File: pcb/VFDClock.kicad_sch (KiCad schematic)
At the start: 80 parts, among them J1 Conn_02x03_Top_Bottom_Mountin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, J2 Conn_02x03_Top_Bottom_Mountin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, J3 USB_C_Receptacle_USB2.0_16P, J4 Conn_02x03_Top_Bottom_Mountin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, J5 Conn_02x03_Top_Bottom_Mountin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, Q1 BSS138, SW1 SW_SPST, SW2 SW_SPST, SW3 SW_SPST, SW4 SW_SPST, SW5 SW_SPST, SW6 SW_SPST, U1 TBD62783AFWG, U10 IP4234CZ6, U11 DS3231MZ+TRL, U2 ESP32-S3-WROOM-1, U3 TBD62783AFNG, U4 SN74HC595PWR, U5 AMS1117-3.3, U6 SHT45-AD1B-R2, U7 AMS1117-1.5, U8 VEML3235SL

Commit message: Added footprints
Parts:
- removed D35: 1PS70SB84, Package_TO_SOT_SMD:SOT-323_SC-70, symbol Diode:BAT54SW
- removed J1, J2, J4, J5: Conn_02x03_Top_Bottom_MountingPin, symbol Connector_Generic_MountingPin:Conn_02x03_Top_Bottom_MountingPin
- removed SW1: SW_SPST, Button_Switch_SMD:SW_SPST_B3U-1000P, symbol Switch:SW_SPST
- added C10, C11, C12, C13: 100n, Capacitor_SMD:C_0805_2012Metric, symbol Device:C
- added C21: 22u, Capacitor_Tantalum_SMD:CP_EIA-3528-15_AVX-H, symbol Device:C_Polarized
- added F1: 3,5 A, Fuse:Fuseholder_Cylinder-5x20mm_Schurter_0031_8201_Horizontal_Open, symbol Device:Fuse
- added J1: Conn_01x04_Socket, Connector_PinSocket_2.54mm:PinSocket_2x02_P2.54mm_Vertical_SMD, symbol Connector:Conn_01x04_Socket
- added J2: L_SIG_CONN, Connector_PinHeader_2.54mm:PinHeader_2x03_P2.54mm_Horizontal, symbol Connector_Generic:Conn_02x03_Top_Bottom
- added J3: L_PWR_CONN, Connector_PinHeader_2.54mm:PinHeader_2x03_P2.54mm_Horizontal, symbol Connector_Generic:Conn_02x03_Top_Bottom
- added J5: R_SIG_CONN, Connector_PinHeader_2.54mm:PinHeader_2x03_P2.54mm_Horizontal, symbol Connector_Generic:Conn_02x03_Top_Bottom
- added J6: R_PWR_CONN, Connector_PinHeader_2.54mm:PinHeader_2x03_P2.54mm_Horizontal, symbol Connector_Generic:Conn_02x03_Top_Bottom
- added J7: Conn_02x06_Top_Bottom, Connector_PinSocket_2.54mm:PinSocket_2x06_P2.54mm_Vertical_SMD, symbol Connector_Generic:Conn_02x06_Top_Bottom
- added SW2: SW_SPST, Button_Switch_SMD:SW_SPST_PTS810, symbol Switch:SW_SPST
- BT1: value Battery_Cell -> CR2032; footprint (none) -> Battery:BatteryHolder_Keystone_3034_1x20mm
- D1: renamed from D3; footprint (none) -> Diode_SMD:D_0603_1608Metric
- D2: footprint (none) -> Diode_SMD:D_0603_1608Metric
- R19: renamed from R21; footprint (none) -> OptoDevice:R_LDR_5.1x4.3mm_P3.4mm_Vertical
- RV1: footprint (none) -> Potentiometer_THT:Potentiometer_Bourns_3339P_Vertical
- SW1: renamed from SW2; footprint Button_Switch_SMD:SW_SPST_B3U-1000P -> Button_Switch_SMD:SW_SPST_PTS810
- SW3, SW4, SW5, SW6: footprint (none) -> Button_Switch_THT:SW_Tactile_SPST_Angled_PTS645Vx83-2LFS
- renumbered C5 to C14, C8 to C15, C13 to C16, C11 to C17, C12 to C18, C9 to C19, C10 to C20, C6 to C5, C7 to C6, C14 to C7, C15 to C8, C16 to C9, D25 to D10, D26 to D11, D33 to D12, D34 to D13, D30 to D3, D27 to D4, D28 to D5, D31 to D6, D32 to D7, D19 to D8, D20 to D9, J3 to J4, R13 to R1, R2 to R10, R3 to R11, R4 to R12, R5 to R13, R6 to R14, R9 to R15, R10 to R16, R11 to R17, R12 to R18, R14 to R2, R7 to R20, R8 to R21, R15 to R3, R16 to R4, R17 to R5, R18 to R6, R19 to R7, R20 to R8, R1 to R9, U7 to U10, U10 to U3, U3 to U4, U4 to U5, U5 to U6, U11 to U7, U6 to U8, U8 to U9
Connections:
- net +3V3: now also J1.1 (Pin_1), J7.1 (Pin_1)
- net +5V: now also C10.1, C11.1, C12.1, C13.1, F1.1, J3.1 (Pin_1), J3.2 (Pin_2), J3.3 (Pin_3), J6.1 (Pin_1), J6.2 (Pin_2), J6.3 (Pin_3), J7.7 (Pin_7); no longer U3.5 (VP)
- net GND: now also C10.2, C11.2, C12.2, C13.2, C21.2, J1.4 (Pin_4), J3.4 (Pin_4), J3.5 (Pin_5), J3.6 (Pin_6), J6.4 (Pin_4), J6.5 (Pin_5), J6.6 (Pin_6), J7.11 (Pin_11), J7.12 (Pin_12), J7.6 (Pin_6), SW2.2 (B)
- net GRID_L1: now also J2.1 (Pin_1)
- net GRID_L2: now also J2.2 (Pin_2)
- net GRID_R1: now also J5.1 (Pin_1)
- net GRID_R2: now also J5.2 (Pin_2)
- net RCLK: now also J2.6 (Pin_6), J5.6 (Pin_6)
- net SER_LEFT: now also J2.3 (Pin_3)
- net SER_RIGHT: now also J5.3 (Pin_3)
- net SRCLK: now also J2.4 (Pin_4), J5.4 (Pin_4)
- net Uphoto: now also U2.8 (IO15)
- net Vbat: now also C21.1
- net /SRCLR: now also J2.5 (Pin_5), J5.5 (Pin_5)
- net at R12.2: now also SW2.1 (A)
- net GPIO3: now reaches U2.15 (IO3)
- net GPIO3: now also J7.2 (Pin_2)
- net GPIO48: now reaches U2.25 (IO48)
- net GPIO48: now also J7.10 (Pin_10)
- net GPIO40: now reaches U2.33 (IO40)
- net GPIO40: now also J7.5 (Pin_5)
- net GPIO41: now reaches U2.34 (IO41)
- net GPIO41: now also J7.8 (Pin_8)
- net GPIO42: now reaches U2.35 (IO42)
- net GPIO42: now also J7.9 (Pin_9)
- net at U2.36 (RXD0): now also J1.3 (Pin_3)
- net at U2.37 (TXD0): now also J1.2 (Pin_2)
- net GPIO16: now reaches U2.9 (IO16)
- net GPIO16: now also J7.3 (Pin_3)
- net TEMP_DATA renamed GPIO39
- net GPIO39: now also J7.4 (Pin_4)
- new net: F1.2, U3.5 (VP)
- no-connect marks 16 -> 12
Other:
- note added: "0,25 mA"
- note added: "0,33 mA"
- note added: "0,5 mA"
- note added: "0,65 mA"
- note added: "144 mA (5 V)"
- note added: "3 mA (25,5 V)"
- note added: "360 mW bez ESP"
- note added: "37 mA"
- note added: "70 mA"
- note added: "Left display connectors"
- note added: "Neopixel decoupling"
- note added: "Right display connectors"
- note added: "UART"
- note removed: "Power budget na 3V3 Board interconnecty"
- moved on the sheet: BT1, C1, C14, C15, C16, C17, C18, C19, C2, C20, C3, C4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

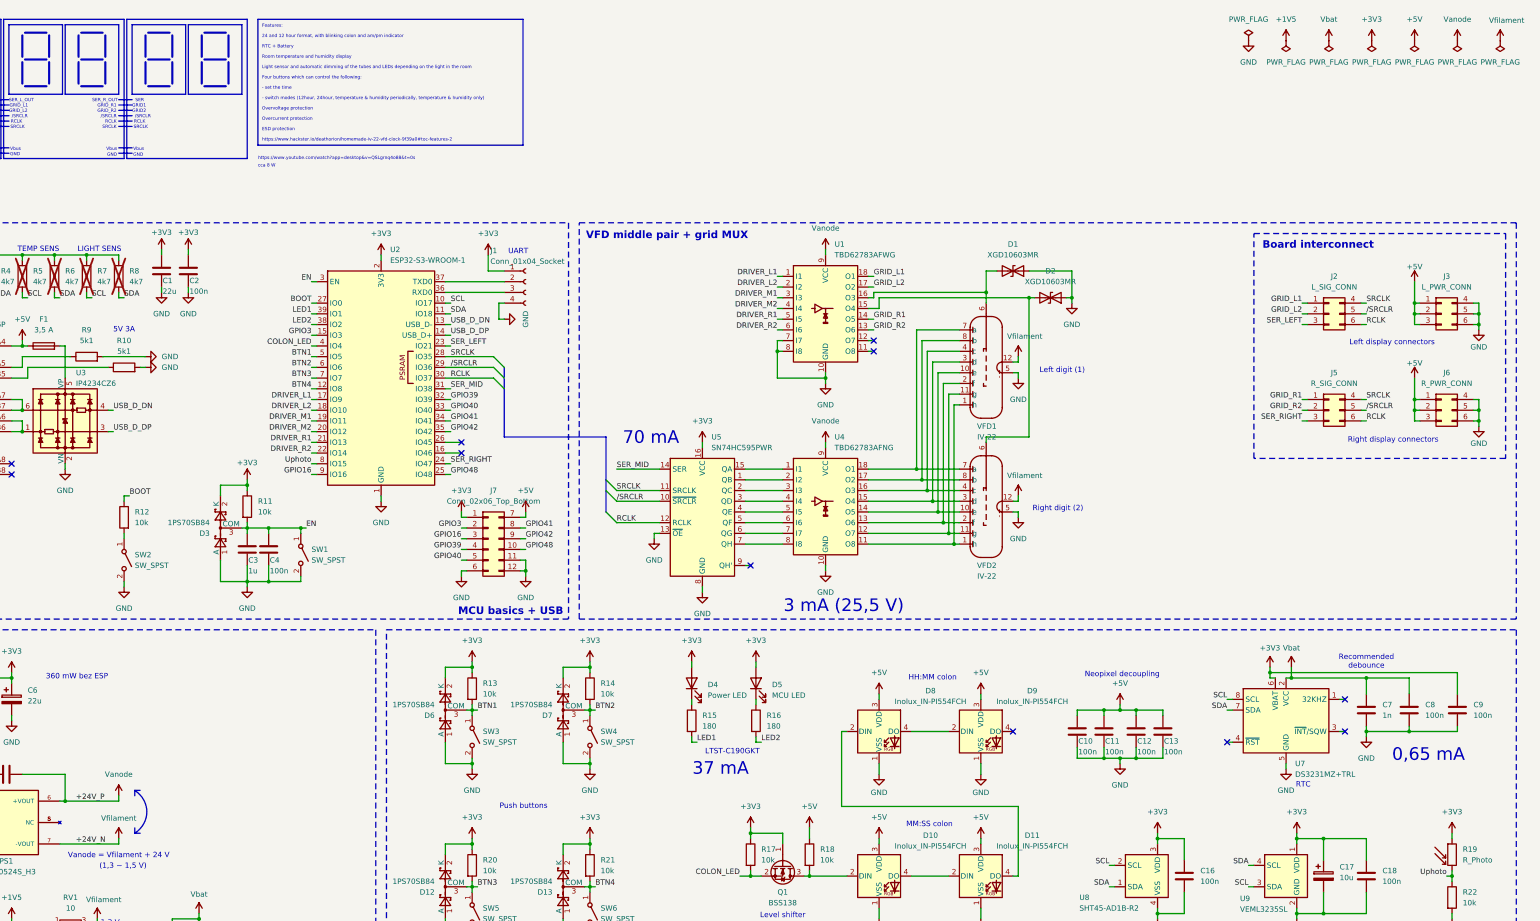
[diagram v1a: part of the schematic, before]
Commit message: Added custom USB-C footprint
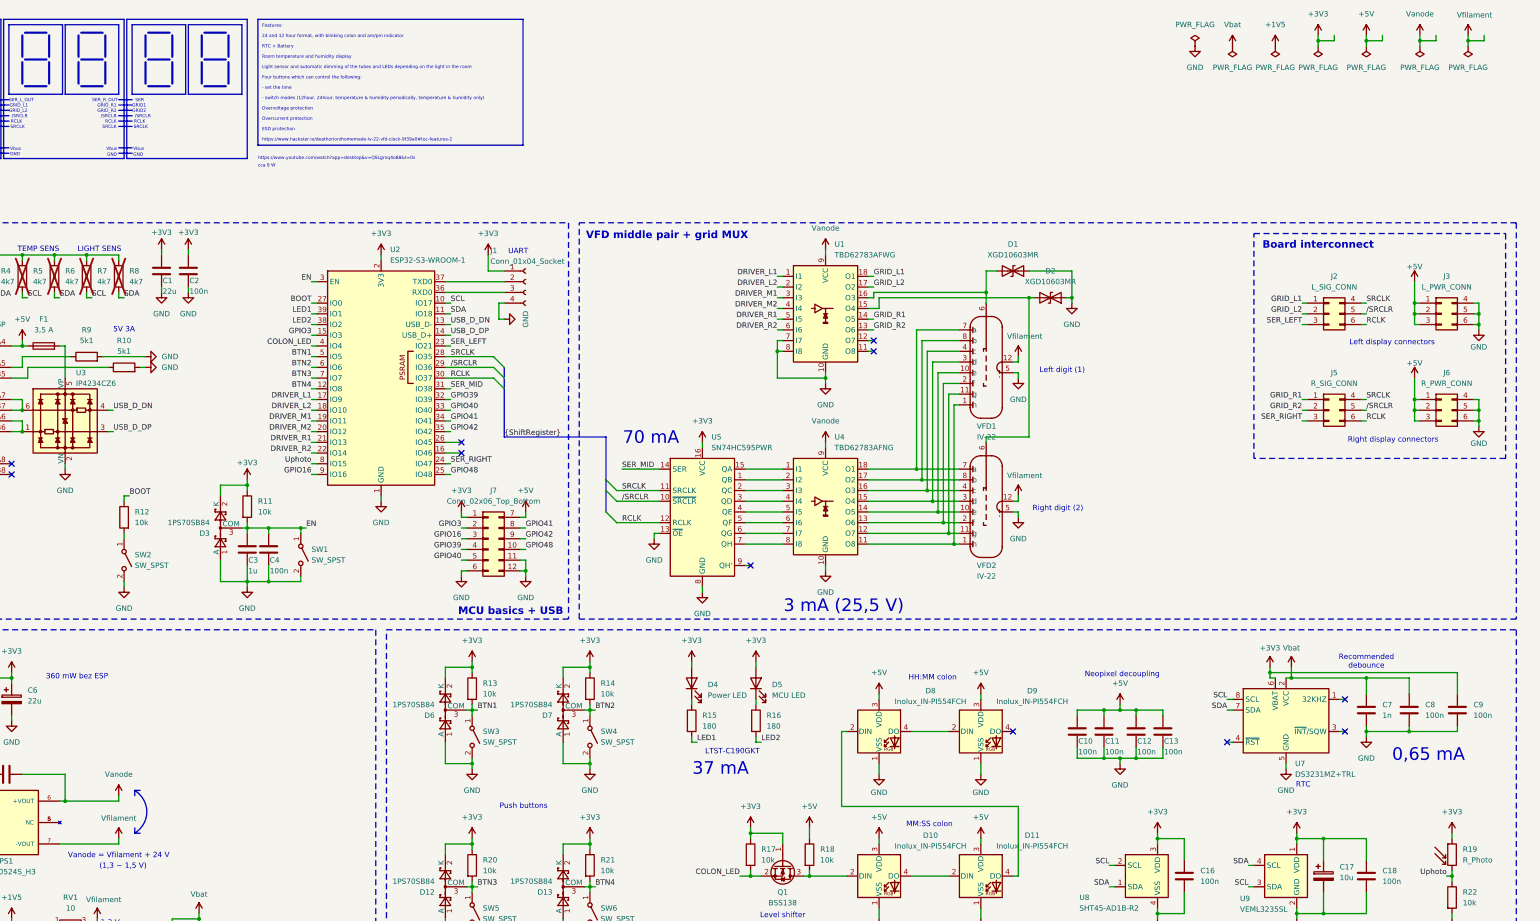
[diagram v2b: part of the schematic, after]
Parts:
- removed VFD1, VFD2: IV-22, Vacuum_Tubes:PL31-A_P_Socket, symbol Vacuum_Tubes:IV-22_VFD_Tube
- added VFD1, VFD2: IV-22, VFDClock_custom_lib:PL31-A_P_Socket, symbol VFDClock_custom_lib:IV-22_VFD_Tube
- J4: footprint Connector_USB:USB_C_Receptacle_GCT_USB4110 -> VFDClock_custom_lib:CUI_UJ20-C-V-C-2-SMT-TR
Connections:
- net GND: now also VFD1.5, VFD2.5
- net Vfilament: now also VFD1.12, VFD2.12
- net at U4.11 (O8): now also VFD1.1 (h), VFD2.1 (h)
- net at U4.14 (O5): now also VFD1.10 (e), VFD2.10 (e)
- net at U4.12 (O7): now also VFD1.11 (g), VFD2.11 (g)
- net at U4.13 (O6): now also VFD1.2 (f), VFD2.2 (f)
- net at U4.15 (O4): now also VFD1.3 (d), VFD2.3 (d)
- net at U4.16 (O3): now also VFD1.4 (c), VFD2.4 (c)
- net at D2.2 (A2), U1.15 (O4): now also VFD2.6
- net at U4.18 (O1): now also VFD1.7 (a), VFD2.7 (a)
- net at U4.17 (O2): now also VFD1.8 (b), VFD2.8 (b)
- net at D1.2 (A2), U1.16 (O3): now also VFD1.6

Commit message: Initial component placement
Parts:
- J2, J3, J5, J6: symbol Connector_Generic:Conn_02x03_Top_Bottom -> Connector_Generic:Conn_02x03_Odd_Even
- J7: symbol Connector_Generic:Conn_02x06_Top_Bottom -> Connector_Generic:Conn_02x06_Odd_Even
- VFD1, VFD2: footprint VFDClock_custom_lib:PL31-A_P_Socket -> Connector_PinSocket_2.54mm:PinSocket_1x12_P2.54mm_Vertical
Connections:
- net +5V: now also J3.5 (Pin_5), J6.5 (Pin_5), J7.2 (Pin_2); no longer J3.2 (Pin_2), J6.2 (Pin_2), J7.7 (Pin_7)
- net DRIVER_L1: now also U1.6 (I6); no longer U1.1 (I1)
- net DRIVER_L2: now also U1.5 (I5); no longer U1.2 (I2)
- net DRIVER_M1: now also U1.4 (I4); no longer U1.3 (I3)
- net DRIVER_M2: now also U1.3 (I3); no longer U1.4 (I4)
- net DRIVER_R1: now also U1.2 (I2); no longer U1.5 (I5)
- net DRIVER_R2: now also U1.1 (I1); no longer U1.6 (I6)
- net GND: now also J3.2 (Pin_2), J6.2 (Pin_2), J7.10 (Pin_10); no longer J3.5 (Pin_5), J6.5 (Pin_5), J7.6 (Pin_6)
- net GPIO16: now also J7.5 (Pin_5); no longer J7.3 (Pin_3)
- net GPIO3: now also J7.3 (Pin_3); no longer J7.2 (Pin_2)
- net GPIO39: now also J7.7 (Pin_7); no longer J7.4 (Pin_4)
- net GPIO40: now also J7.9 (Pin_9); no longer J7.5 (Pin_5)
- net GPIO41: now also J7.4 (Pin_4); no longer J7.8 (Pin_8)
- net GPIO42: now also J7.6 (Pin_6); no longer J7.9 (Pin_9)
- net GPIO48: now also J7.8 (Pin_8); no longer J7.10 (Pin_10)
- net GRID_L1: now also U1.13 (O6); no longer U1.18 (O1)
- net GRID_L2: now also J2.3 (Pin_3), U1.14 (O5); no longer J2.2 (Pin_2), U1.17 (O2)
- net GRID_R1: now also U1.17 (O2); no longer U1.14 (O5)
- net GRID_R2: now also J5.3 (Pin_3), U1.18 (O1); no longer J5.2 (Pin_2), U1.13 (O6)
- net SER_LEFT: now also J2.5 (Pin_5); no longer J2.3 (Pin_3)
- net SER_RIGHT: now also J5.5 (Pin_5); no longer J5.3 (Pin_3)
- net SRCLK: now also J2.2 (Pin_2), J5.2 (Pin_2); no longer J2.4 (Pin_4), J5.4 (Pin_4)
- net /SRCLR: now also J2.4 (Pin_4), J5.4 (Pin_4); no longer J2.5 (Pin_5), J5.5 (Pin_5)
- net at D1.2 (A2), VFD1.6: now also U1.15 (O4); no longer U1.16 (O3)
- net at D2.2 (A2), VFD2.6: now also U1.16 (O3); no longer U1.15 (O4)

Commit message: Footprint placement progress
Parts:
- removed C21: 22u, Capacitor_Tantalum_SMD:CP_EIA-3528-15_AVX-H, symbol Device:C_Polarized
- removed R3, R4: 4k7, Resistor_SMD:R_0805_2012Metric, symbol Device:R
- D4: footprint Diode_SMD:D_0603_1608Metric -> LED_SMD:LED_0603_1608Metric
- U9: footprint VFDClock_custom_lib:VEML3235SL_Vertical -> VFDClock_custom_lib:VEML3235SL_Horizontal
- renumbered C19 to C20, C20 to C21, R12 to R10, R13 to R11, R14 to R12, R15 to R13, R16 to R14, R17 to R15, R18 to R16, R19 to R17, R20 to R18, R21 to R19, R22 to R20, R5 to R3, R6 to R4, R7 to R5, R8 to R6, R9 to R7, R10 to R8, R11 to R9
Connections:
- net BTN4: now also U2.8 (IO15); no longer U2.12 (IO8)
- net SRCLK: now also U2.29 (IO36); no longer U2.28 (IO35)
- net Uphoto: now also U2.9 (IO16); no longer U2.8 (IO15)
- net /SRCLR: now also U2.28 (IO35); no longer U2.29 (IO36)
- net GPIO16 renamed GPIO8
- net GPIO8: now also U2.12 (IO8); no longer U2.9 (IO16)
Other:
- moved on the sheet: R3, R4, R5, R6

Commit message: Footprint placement done, PWR needs connecting
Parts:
- removed C10, C11, C12, C13: 100n, Capacitor_SMD:C_0805_2012Metric, symbol Device:C
- removed D10, D11, D8, D9: Inolux_IN-PI554FCH, LED_SMD:LED_Inolux_IN-PI554FCH_PLCC4_5.0x5.0mm_P3.2mm, symbol LED:Inolux_IN-PI554FCH
- removed J7: Conn_02x06_Top_Bottom, Connector_PinSocket_2.54mm:PinSocket_2x06_P2.54mm_Vertical_SMD, symbol Connector_Generic:Conn_02x06_Odd_Even
- removed Q1: BSS138, Package_TO_SOT_SMD:SOT-23, symbol Transistor_FET:BSS138
- removed R15, R16: 10k, Resistor_SMD:R_0805_2012Metric, symbol Device:R
- added C17, C20, C5, C8: 100n, Capacitor_SMD:C_0805_2012Metric, symbol Device:C
- added J7: CONN_GPIO, Connector_PinSocket_2.54mm:PinSocket_2x04_P2.54mm_Vertical_SMD, symbol Connector_Generic:Conn_02x04_Odd_Even
- added J8: L_COL_CONN, Connector_JST:JST_XH_B4B-XH-A_1x04_P2.50mm_Vertical, symbol Connector_Generic:Conn_02x02_Odd_Even
- added J9: R_COL_CONN, Connector_JST:JST_XH_B4B-XH-A_1x04_P2.50mm_Vertical, symbol Connector_Generic:Conn_02x02_Odd_Even
- added R7, R8: 100k, Resistor_SMD:R_0805_2012Metric, symbol Device:R
- F1: value 3,5 A -> 2,5 A Fast Blow; footprint Fuse:Fuseholder_Cylinder-5x20mm_Schurter_0031_8201_Horizontal_Open -> Fuse:Fuse_0603_1608Metric
- renumbered C8 to C10, C9 to C11, C14 to C12, C15 to C13, C16 to C14, C17 to C15, C18 to C16, C20 to C18, C21 to C19, C5 to C6, C6 to C7, C7 to C9, D12 to D8, D13 to D9, R7 to R10, R9 to R11, R10 to R12, R11 to R13, R12 to R14, R13 to R15, R14 to R16, R8 to R9
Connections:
- net +1V5: now also C20.1
- net +3V3: now also C8.1, J7.7 (Pin_7), J8.1 (Pin_1), J9.1 (Pin_1)
- net +5V: now also F1.2, U3.5 (VP), C17.1, C5.1, J7.8 (Pin_8), J8.3 (Pin_3), J9.3 (Pin_3); no longer F1.1, J4.A4 (VBUS), J4.A9 (VBUS), J4.B4 (VBUS), J4.B9 (VBUS)
- net COLON_LED: now also J8.2 (Pin_2), J9.2 (Pin_2)
- net GND: now also J1.3 (Pin_3), R10.1, R9.1, C17.2, C20.2, C5.2, C8.2, J7.6 (Pin_6), J8.4 (Pin_4), J9.4 (Pin_4); no longer J1.4 (Pin_4), R10.2, R9.2
- net GPIO3: now also R7.1
- net GPIO39: now also J7.2 (Pin_2)
- net GPIO40: now also J7.5 (Pin_5)
- net GPIO41: now also J7.3 (Pin_3)
- net GPIO42: now also J7.1 (Pin_1)
- net GPIO48: now also R8.1
- net GPIO8: now also J7.4 (Pin_4)
- net GRID_L2: now also J2.2 (Pin_2); no longer J2.3 (Pin_3)
- net GRID_R2: now also J5.2 (Pin_2); no longer J5.3 (Pin_3)
- net RCLK: now also J2.3 (Pin_3), J5.3 (Pin_3); no longer J2.6 (Pin_6), J5.6 (Pin_6)
- net SER_LEFT: now also J2.6 (Pin_6); no longer J2.5 (Pin_5)
- net SER_RIGHT: now also J5.6 (Pin_6); no longer J5.5 (Pin_5)
- net SRCLK: now also J2.4 (Pin_4), J5.4 (Pin_4); no longer J2.2 (Pin_2), J5.2 (Pin_2)
- net /SRCLR: now also J2.5 (Pin_5), J5.5 (Pin_5); no longer J2.4 (Pin_4), J5.4 (Pin_4)
- net at J4.A5 (CC1): now also R10.2, R7.2; no longer R10.1
- net at J4.B5 (CC2): now also R9.2, R8.2; no longer R9.1
- net at U2.36 (RXD0): now also J1.4 (Pin_4); no longer J1.3 (Pin_3)
- new net: F1.1, J4.A4 (VBUS), J4.A9 (VBUS), J4.B4 (VBUS), J4.B9 (VBUS)
- no-connect marks 12 -> 11
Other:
- note removed: "HH:MM colon"
- note removed: "Level shifter"
- note removed: "MM:SS colon"
- note removed: "Neopixel decoupling"
- moved on the sheet: BT1, C18, C19, C6, C7, F1, R10, R9, RV1, U10, U6

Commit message: Layout done, generated fabrication files
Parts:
- removed C1: 22u, Capacitor_SMD:C_0805_2012Metric, symbol Device:C
- added C1: 10u, Capacitor_Tantalum_SMD:CP_EIA-3216-18_Kemet-A, symbol Device:C_Polarized
- added H1, H2, H3: MountingHole_Pad, MountingHole:MountingHole_3.2mm_M3_ISO14580_Pad_TopBottom, symbol Mechanical:MountingHole_Pad
- J2: value L_SIG_CONN -> R_SIG_CONN
- J5: value R_SIG_CONN -> L_SIG_CONN
- R17, R20: now not fitted
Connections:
- net +3V3: now also C1.1
- net GND: now also C1.2, H1.1, H2.1, H3.1
- net SER_LEFT: now also J5.6 (Pin_6), U2.24 (IO47); no longer J2.6 (Pin_6), U2.23 (IO21)
- net SER_RIGHT: now also J2.6 (Pin_6), U2.23 (IO21); no longer J5.6 (Pin_6), U2.24 (IO47)
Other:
- moved on the sheet: J2, J5

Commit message: Modified circuit to use synchronous grid clock on all modules
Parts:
- J3: value L_PWR_CONN -> R_PWR_CONN
- J6: value R_PWR_CONN -> L_PWR_CONN
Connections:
- net GND: now also U1.1 (I1), U1.2 (I2), U1.5 (I5), U1.6 (I6)
- net GRID_1: now reaches D1.2 (A2), U1.15 (O4), VFD1.6
- net GRID_1: now also J2.1 (Pin_1), J5.1 (Pin_1)
- net GRID_2: now reaches D2.2 (A2), U1.16 (O3), VFD2.6
- net GRID_2: now also J2.2 (Pin_2), J5.2 (Pin_2)
- net DRIVER_L1: no longer names the net of U2.17 (IO9)
- net DRIVER_L1: no longer U1.6 (I6)
- net DRIVER_L2: no longer names the net of U2.18 (IO10)
- net DRIVER_L2: no longer U1.5 (I5)
- net DRIVER_M1 renamed DRIVER_1
- net DRIVER_M2 renamed DRIVER_2
- net DRIVER_R1: no longer names the net of U2.21 (IO13)
- net DRIVER_R1: no longer U1.2 (I2)
- net DRIVER_R2: no longer names the net of U2.22 (IO14)
- net DRIVER_R2: no longer U1.1 (I1)
- net GRID_L1: no longer names the net of U1.13 (O6)
- net GRID_L1: no longer J2.1 (Pin_1)
- net GRID_L2: no longer names the net of U1.14 (O5)
- net GRID_L2: no longer J2.2 (Pin_2)
- net GRID_R1: no longer names the net of U1.17 (O2)
- net GRID_R1: no longer J5.1 (Pin_1)
- net GRID_R2: no longer names the net of U1.18 (O1)
- net GRID_R2: no longer J5.2 (Pin_2)
- no-connect marks 11 -> 19
